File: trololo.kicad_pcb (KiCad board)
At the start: 4 copper layers, 135.6 x 54.6 mm, 104 parts, among them J1 10118194-0001LF, J10 Conn_02x12_Odd_Even, J11 Conn_02x02_Odd_Even, J12 VBATJ, J13 PROTO1, J18 PROTO1, J2 10118194-0001LF, J3 RJ45_Amphenol_RJMG1BD3B8K1ANR, J4 Micro_SD_Card, J5 Screw_Terminal_01x06, J6 Conn_02x12_Odd_Even, J7 10118194-0001LF, J8 Screw_Terminal_01x02, J9 Conn_02x12_Odd_Even, SW1 RESET, SW2 PC13, U1 STM32H743VITx, U10 USBLC6-2SC6, U11 SN6505, U12 TCAN332, U13 ISL83483, U2 KSZ8081RNA, U3 ISO1050DUB, U4 ISO3082DW, U5 S25FL127SABMFI101, U6 AP63203, U7 USBLC6-2SC6, U8 STM32F042F6Px, U9 USBLC6-2SC6, Y1 8MHz, Y2 32.768KHz, Y3 25MHz

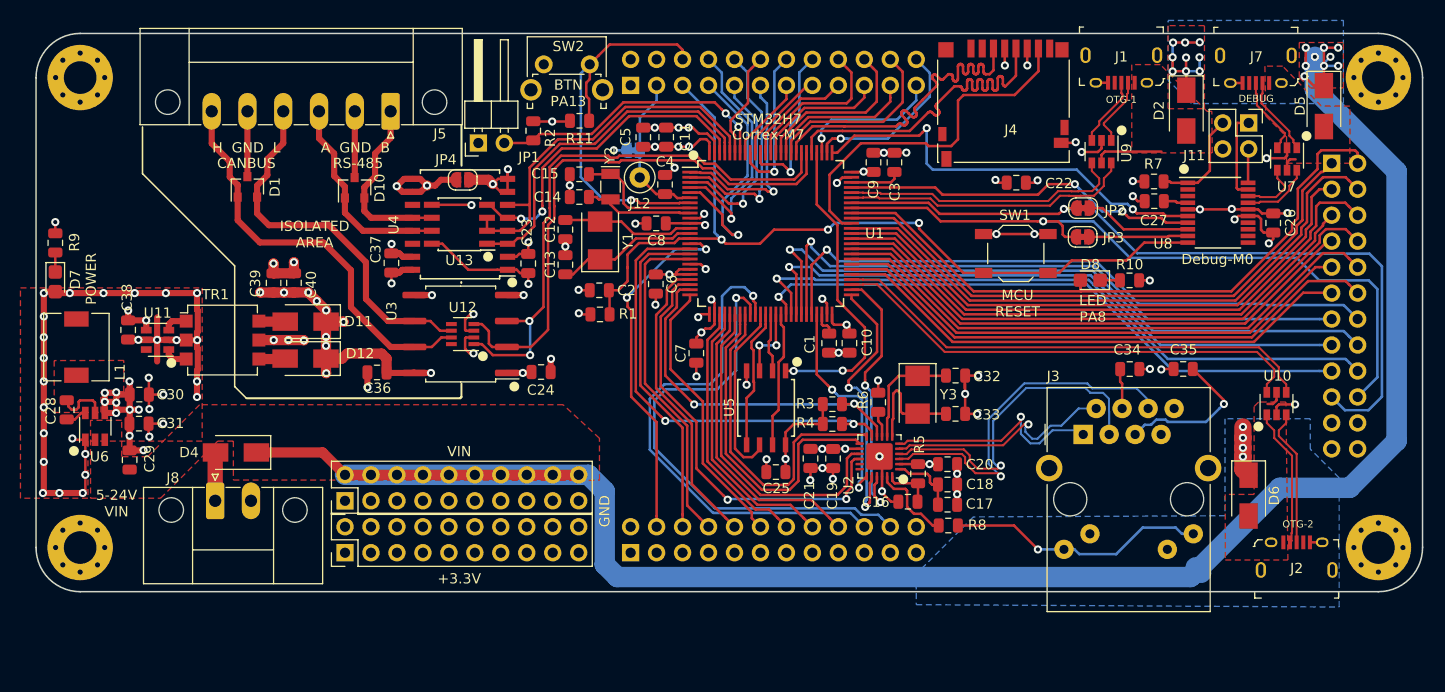
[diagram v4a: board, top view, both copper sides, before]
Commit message: Add battery pins
Signed-off-by: Martin Ribelotta <martinribelotta@gmail.com>
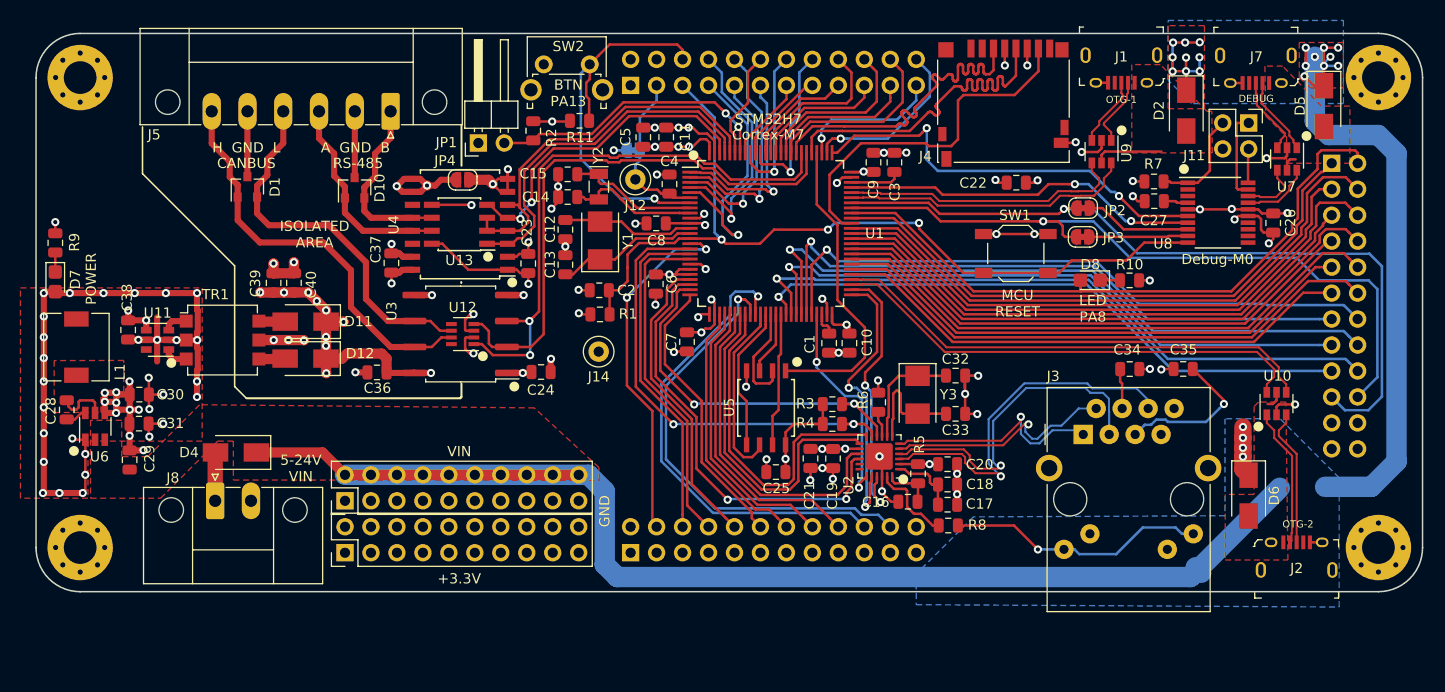
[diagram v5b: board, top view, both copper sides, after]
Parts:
- added J14: VBATG, TestPoint:TestPoint_Loop_D1.80mm_Drill1.0mm_Beaded, F.Cu at (113.7, 59.1)
- J12: value VBATJ -> VBAT+
- moved C7 1.43 mm to (122.4, 58.1)
- moved C14 1.14 mm to (110.7, 43.9)
- moved C15 1.14 mm to (110.7, 41.7)
- moved Y2 1.14 mm to (113.7, 42.9)
- moved J12 0.46 mm to (117.3, 42.2)
- moved C4 0.44 mm to (120.6, 42.7)
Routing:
- net /QSPI_IO1: track 5.77 -> 10.3 mm
- net /PB0: track 49.8 -> 45.6 mm
- net /PB1: track 50.3 -> 46.4 mm
- net Net-(C14-Pad1): track 10.8 -> 13.0 mm
- net GND: track 135.3 -> 136.8 mm, vias 65 -> 66
- net /RS485_RX: track 34.4 -> 35.7 mm
- net /PC13: track 40.0 -> 38.9 mm
- net /QSPI_IO2: track 7.24 -> 6.20 mm, vias 2 -> 0
- net /ENET_TXD0: track 27.4 -> 28.3 mm
- net +BATT: track 15.5 -> 16.2 mm
- net /~QSPI_CS: vias 2 -> 0

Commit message: Add logos and change reset button and user led position
Signed-off-by: Martin Ribelotta <martinribelotta@gmail.com>
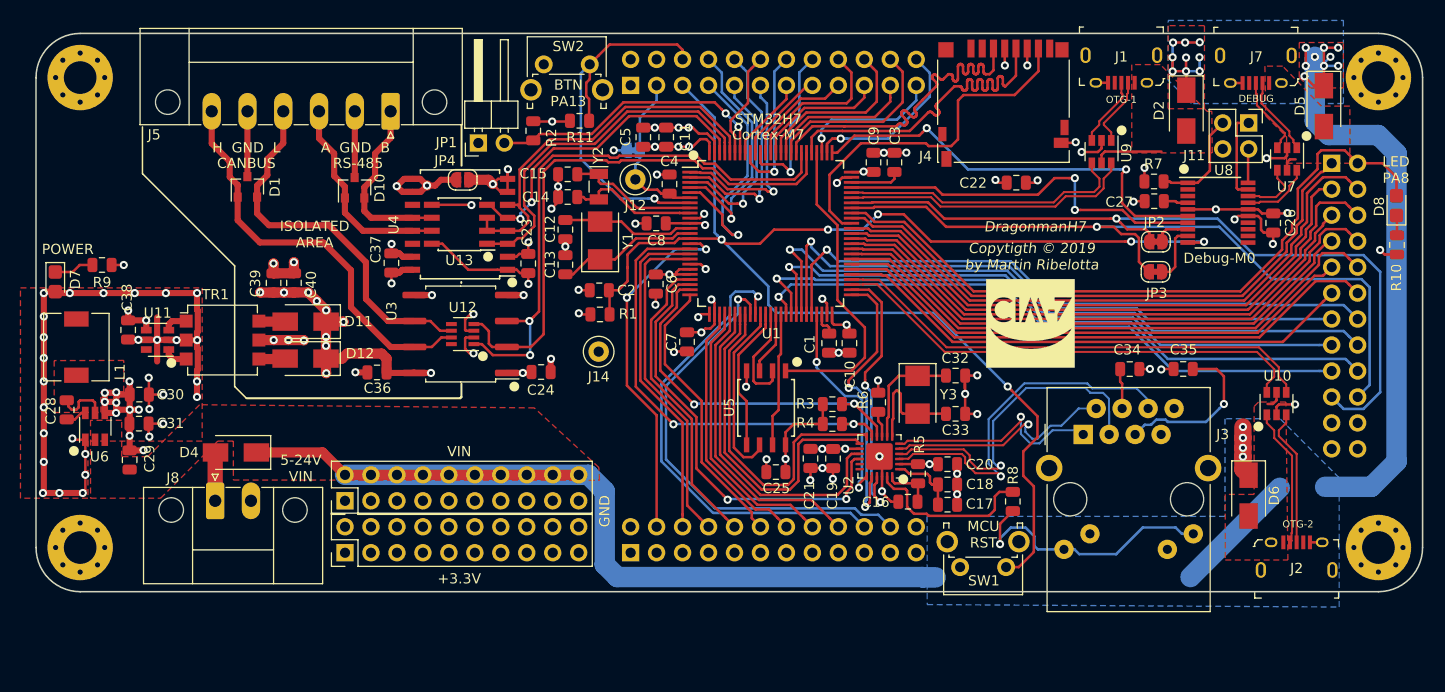
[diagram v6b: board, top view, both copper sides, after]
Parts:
- added G***: LOGO, footprints:ciaa_7-logo, F.Cu at (156.0, 56.3)
- SW1: footprint Button_Switch_SMD:SW_SPST_TL3342 -> Buttons_Switches_THT:SW_Tactile_SPST_Angled_PTS645Vx31-2LFS
- SW2: footprint Button_Switch_THT:SW_Tactile_SPST_Angled_PTS645Vx31-2LFS -> Buttons_Switches_THT:SW_Tactile_SPST_Angled_PTS645Vx31-2LFS
- moved D8 30.8 mm to (191.8, 44.8), turned to 90 degrees
- moved SW1 30.7 mm to (153.6, 80.1), turned to 180 degrees
- moved R10 26.4 mm to (191.8, 48.6), turned to 90 degrees
- moved JP3 7.90 mm to (168.2, 51.3)
- moved JP2 7.84 mm to (168.2, 48.3)
- moved R8 6.74 mm to (154.2, 73.7), turned to 90 degrees
- moved R9 5.06 mm to (65.1, 50.6), turned to 180 degrees
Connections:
- J1 pad 4: Net-(J1-Pad4) -> (no net)
- J2 pad 4: Net-(J2-Pad4) -> (no net)
- J3 pad R7: Net-(J3-PadR7) -> (no net)
- J4 pad 1: Net-(J4-Pad1) -> (no net)
- J4 pad 2: Net-(J4-Pad2) -> (no net)
- J4 pad 8: Net-(J4-Pad8) -> (no net)
- J7 pad 4: Net-(J7-Pad4) -> (no net)
- SW1 pad 1: GND -> /~RESET
- SW1 pad 2: /~RESET -> GND
- U11 pad 6: Net-(U11-Pad6) -> (no net)
- U12 pad 5: Net-(U12-Pad5) -> (no net)
- U12 pad 8: Net-(U12-Pad8) -> (no net)
- U2 pad 17: Net-(U2-Pad17) -> (no net)
- U2 pad 18: Net-(U2-Pad18) -> (no net)
- U4 pad 11: Net-(U4-Pad11) -> (no net)
- U4 pad 14: Net-(U4-Pad14) -> (no net)
- U8 pad 11: Net-(U8-Pad11) -> (no net)
- U8 pad 12: Net-(U8-Pad12) -> (no net)
- U8 pad 13: Net-(U8-Pad13) -> (no net)
- U8 pad 14: Net-(U8-Pad14) -> (no net)
- U8 pad 2: Net-(U8-Pad2) -> (no net)
- U8 pad 3: Net-(U8-Pad3) -> (no net)
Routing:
- net /~RESET: track 83.9 -> 141.8 mm, vias 3 -> 6
- net VDC: track 224.0 -> 198.4 mm
- net /ETH_LED: track 8.31 -> 16.9 mm
- net /U2_TX: track 10.4 -> 3.47 mm
- net GND: track 136.8 -> 131.0 mm, vias 66 -> 64
- net /PA8: track 63.5 -> 68.6 mm
- net /U2_RX: track 9.67 -> 5.58 mm
- net /U1_TX: track 70.4 -> 73.5 mm
- net /SWDIO: track 35.2 -> 37.5 mm
- net /U1_RX: track 74.9 -> 76.9 mm
- net Net-(D7-Pad1): track 1.91 -> 3.92 mm
- net Net-(C35-Pad2): track 14.8 -> 16.2 mm
- net Net-(J3-PadL1): track 25.5 -> 26.6 mm
- net /SWCLK: track 41.2 -> 41.8 mm
- net +3V3: track 158.3 -> 158.5 mm, vias 55 -> 54
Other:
- board text added: "Copytigth © 2019 by Martin Ribelotta"
- board text added: "DragonmanH7"
- board text added: "MCU RST"
- board text removed: "MCU RESET"

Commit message: Add packages 3d and last minutes touchs
Signed-off-by: Martin Ribelotta <martinribelotta@gmail.com>
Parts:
- moved G*** 8.09 mm to (155.0, 48.3)
- moved D8 7.50 mm to (191.2, 52.3)
- moved R10 7.50 mm to (191.2, 56.1)
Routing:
- net /PA8: track 68.6 -> 75.3 mm
- net VDC: track 198.4 -> 197.7 mm
